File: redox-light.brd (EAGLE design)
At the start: 162.3 x 129 mm, 136 parts, among them IC36 STM32F103TXUX, IC38 74HC595BQ, IC39 W25Q64FV, X1 USBMICRO_B, X2 AUDIO-JACKSMD

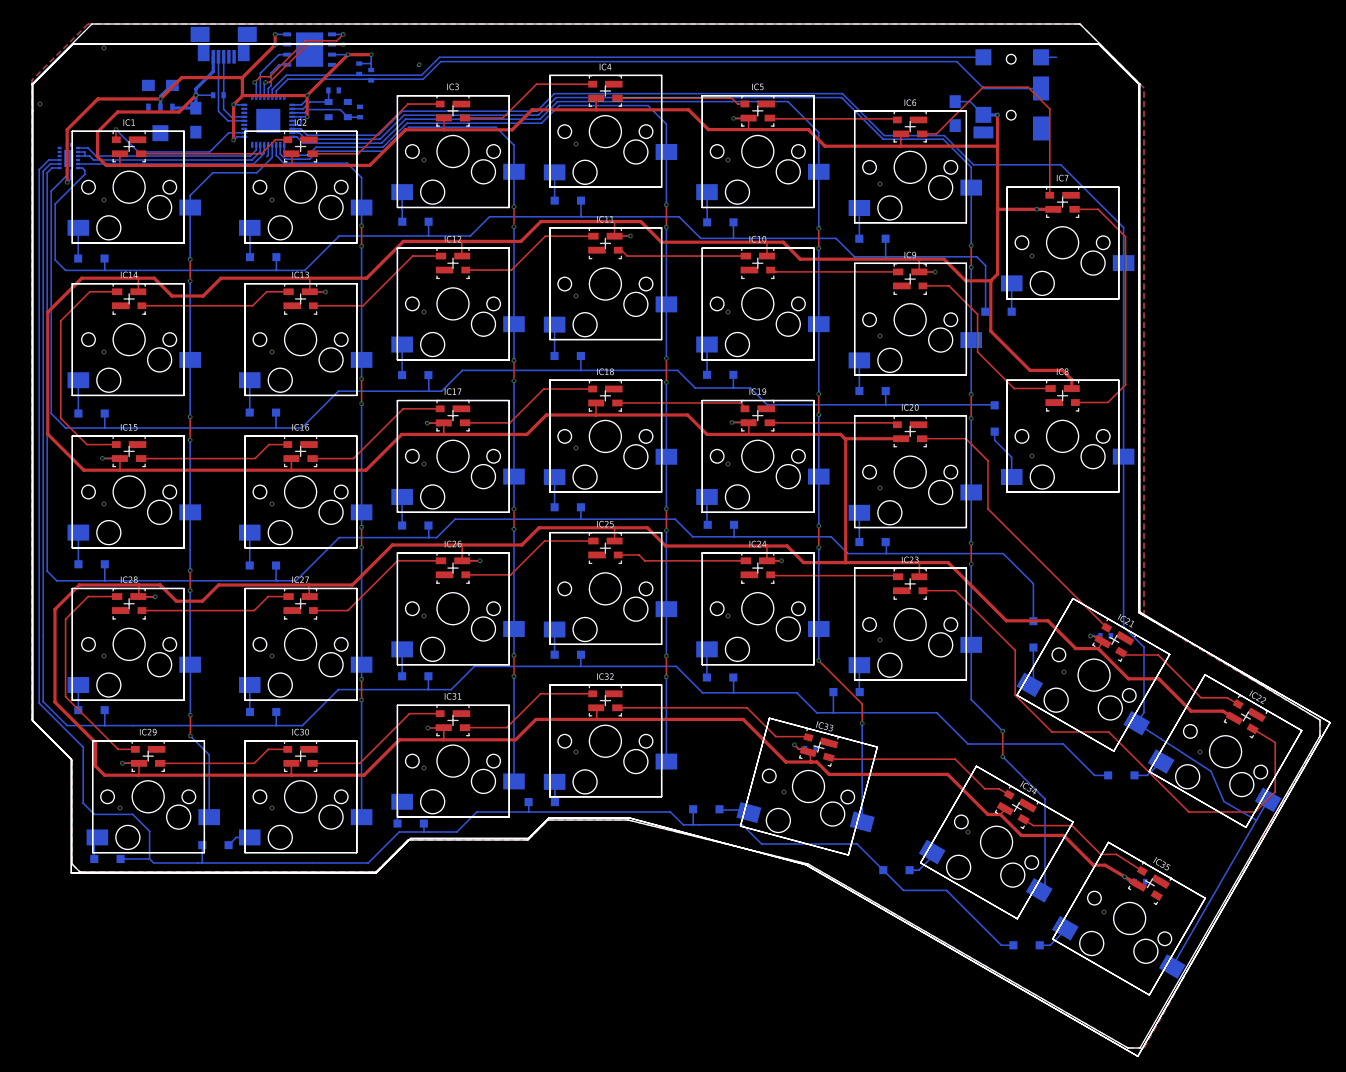
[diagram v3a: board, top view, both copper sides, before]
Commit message: make schematic more simply, added SWD connector
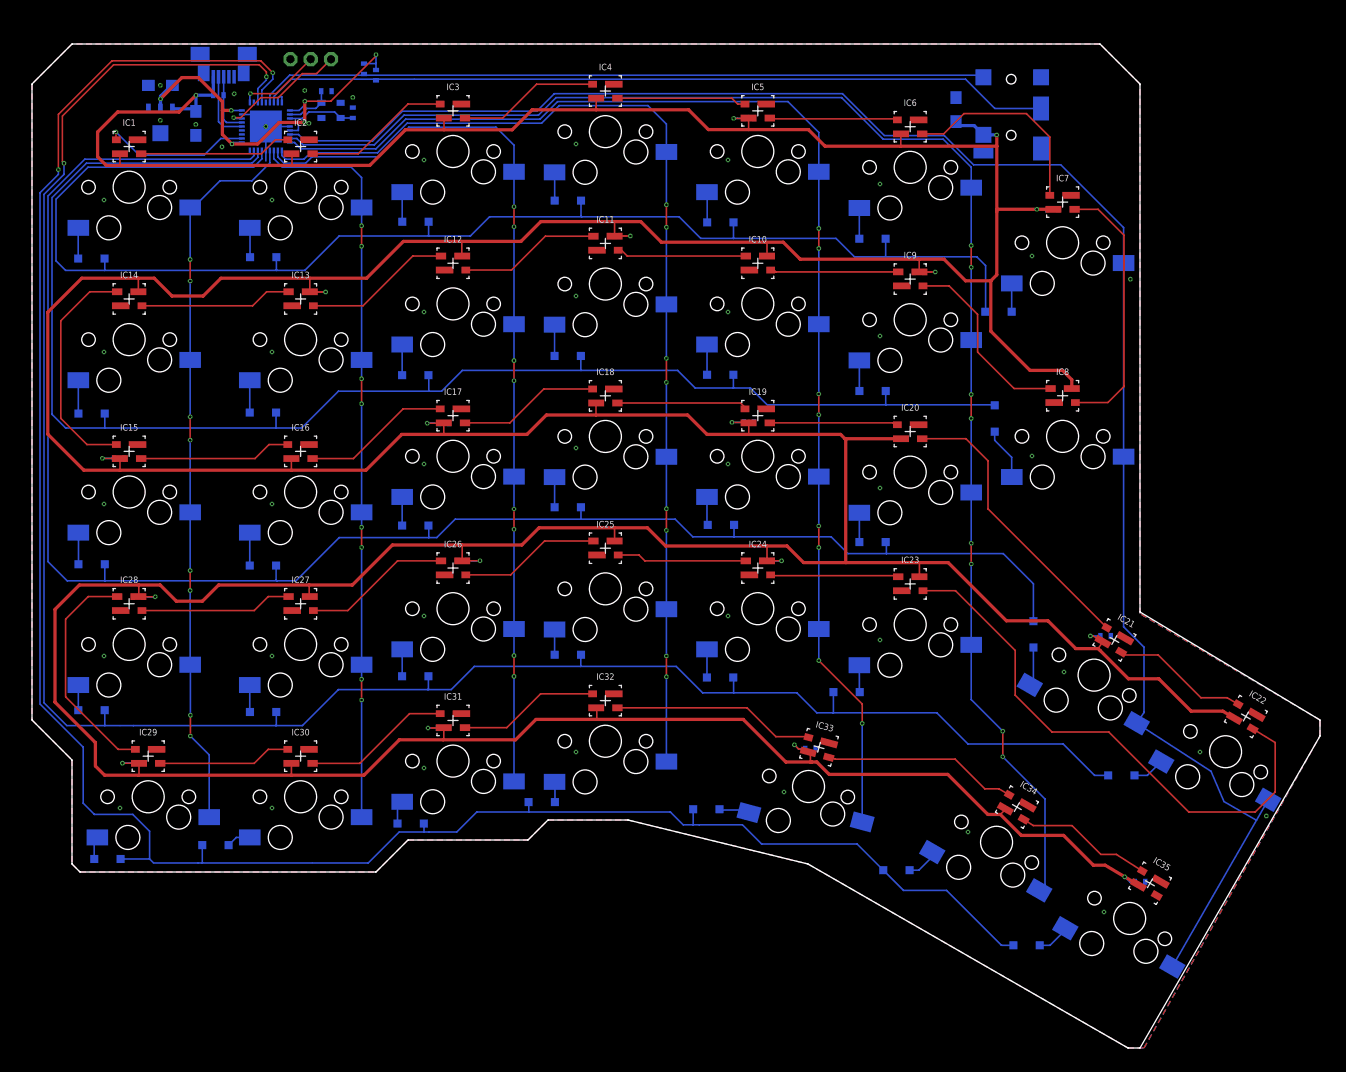
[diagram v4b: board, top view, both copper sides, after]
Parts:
- removed IC38: 74HC595BQ, netcat:DHVQFN16
- removed IC39: W25Q64FV, netcat:WSON8
- added X3: (no value), netcat:1X03
- moved X1 2.50 mm to (19.0, 118.2)
- moved X2 2.50 mm to (117.4, 111.9)
- moved QZ1 0.91 mm to (32.3, 111.2)
- moved C20 0.91 mm to (31.8, 113.6)
- moved C21 0.91 mm to (35.1, 110.9)
- moved IC36 0.76 mm to (24.2, 109.2)
- moved R2 0.60 mm to (36.5, 116.4)
- moved R3 0.60 mm to (38.0, 115.6)
- moved C19 0.51 mm to (110.5, 111.3), turned to 90 degrees
- moved C1 0.40 mm to (15.5, 109.6)
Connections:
- removed net FLASH_CS: IC36.29, IC39.1
- removed net SPI_MISO: IC36.31, IC39.2
- removed net SPI_MOSI: IC36.32, IC39.5
- removed net SPI_SCL: IC36.30, IC39.6
- removed net SR_CLK: IC36.16, IC38.11, IC38.12
- removed net SR_CLR: IC36.17, IC38.10
- removed net SR_D: IC36.15, IC38.14
- net GND: now also X3.1; no longer IC38.13, IC38.8, IC38.PAD, IC39.4
- net ROW0: now also IC36.15; no longer IC38.15
- net ROW1: now also IC36.16; no longer IC38.1
- net ROW2: now also IC36.17; no longer IC38.2
- net ROW3: now also IC36.30; no longer IC38.3
- net ROW4: now also IC36.31; no longer IC38.4
- net SWD_CLK: now also X3.2
- net SWD_IO: now also X3.3
- net VCC: no longer IC38.16, IC39.3, IC39.7, IC39.8
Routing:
- net ROW4: track 225.7 -> 264.9 mm, vias 0 -> 2
- net ROW3: track 223.1 -> 261.5 mm, vias 0 -> 2
- net VCC: track 90.4 -> 57.4 mm, vias 10 -> 6
- net SR_CLK: track 25.6 -> 0.00 mm
- net SR_D: track 24.9 -> 0.00 mm
- net ROW1: track 165.5 -> 190.1 mm
- net SR_CLR: track 23.7 -> 0.00 mm
- net ROW2: track 196.6 -> 219.6 mm
- net ROW0: track 152.9 -> 175.6 mm
- net FLASH_CS: track 16.8 -> 0.00 mm, vias 2 -> 0
- net SWD_IO: track 0.00 -> 16.3 mm, vias 0 -> 1
- net SPI_MISO: track 14.9 -> 0.00 mm, vias 2 -> 0
- net SWD_CLK: track 0.00 -> 10.5 mm, vias 0 -> 1
- net GND: track 3.50 -> 12.7 mm, vias 37 -> 45
- net SPI_SCL: track 7.27 -> 0.00 mm
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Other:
- board size 162.3 x 129 mm -> 161 x 125.5 mm

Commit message: silk layer update
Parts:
- removed C19: 10u, netcat:SMC_A
- added C22: 100n, netcat:R0402
- added U$1: (no value), netcat:LOGO2
- C10, C11, C12, C13, C14, C15, C16, C17, C18, C3, C4, C5, C6, C7, C8, C9: value (none) -> 100n
- moved C15 3.80 mm to (4.60, 29.6), turned to 0 degrees
- moved C10 3.80 mm to (80.8, 72.2), turned to 0 degrees
- moved C9 3.80 mm to (42.7, 72.1), turned to 0 degrees
- moved C8 3.75 mm to (2.15, 67.7), turned to 0 degrees
- moved C17 3.70 mm to (88.6, 31.5), turned to 0 degrees
- moved C4 3.70 mm to (118.9, 98.8), turned to 0 degrees
- moved C16 3.60 mm to (42.8, 34.0), turned to 0 degrees
- moved C14 3.60 mm to (125.6, 45.5), turned to 0 degrees
- moved C3 3.60 mm to (81.0, 110.2), turned to 0 degrees
- moved C18 3.56 mm to (130.0, 15.4), turned to 0 degrees
- moved C12 0.50 mm to (49.3, 54.9)
- moved C11 0.40 mm to (8.70, 50.4)
- moved C5 0.30 mm to (30.0, 88.5)
- moved C6 0.30 mm to (68.1, 95.5)
- moved C7 0.30 mm to (106.2, 91.0)
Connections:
- removed net UART_RX: IC36.22
- removed net UART_TX: IC36.21
- net 5V: no longer C19.+
- net GND: now also C22.2; no longer C19.-
- net VCC: now also C22.1
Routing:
- net 5V: track 891.9 -> 882.3 mm
- net COL0: track 91.0 -> 92.7 mm
- net VCC: track 57.4 -> 58.9 mm
- net GND: vias 45 -> 46
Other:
- board text added: "github.com/netcatu"
- board text added: "redox-light"
- board text added: "v1.0.0"
